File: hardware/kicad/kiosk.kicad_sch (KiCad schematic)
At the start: 16 parts, among them J10 Jack 5V rail 1, J11 Jack 5V rail 2, J13 PCF8574 - han day tu hang P, J14 LCD microSD - lo cho, chua no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, J3 LCD 4.0in ST7796S + GT911, J4 VL53L1X, J5 PCF8574 - de cam 4 chan nguon, J6 DS3231, J7 MAX98357A, J9 SG90 servo, U1 ESP32-S3-CAM N16R8

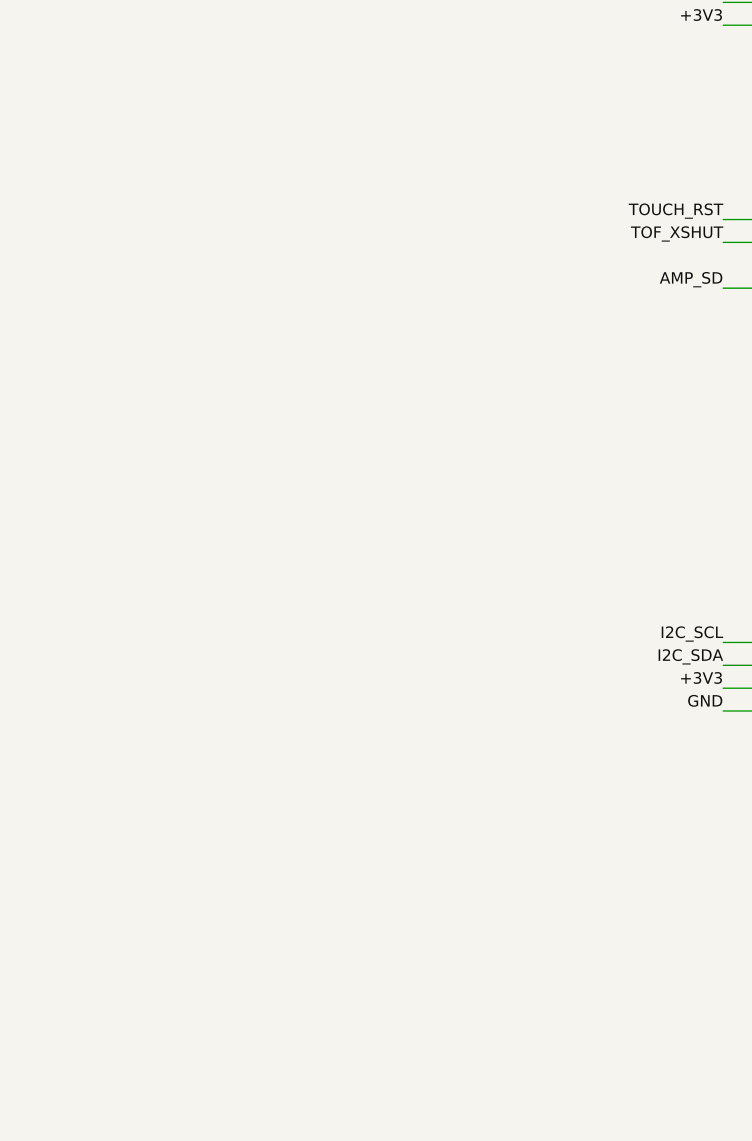
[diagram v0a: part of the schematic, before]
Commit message: feat(hardware): add two USB power inlets beside the terminals
A bench supply now reaches the board over USB as well as through the screw
terminals. Each inlet is two parts: four holes with no net on them at all,
which a breakout solders onto so it cannot come loose, and a pair of holes
above it carrying the rail, which two short wires from the breakout's VBUS
and GND reach.

The anchor row carries no net on purpose. Cheap USB breakouts follow no pin
standard - micro-USB is usually five pins, USB-C ships as two, six and
sixteen, and VBUS and GND sit adjacent on some and at opposite ends on
others - so any net assigned there would encode a guess. Wiring the power
by hand costs two solder joints and works with every one of them.

USB-C feeds rail 1 and micro-USB feeds rail 2, because a C connector is
rated 3 A against rail 1's 1.34 A peak while micro-B is rated 1.8 A and
suits the servo's 0.7 A.

C1, J10 and J11 move 3 mm right to open the pocket. It is a translation, so
every distance the section 2.5 rules name is unchanged, including the
11.5 mm between the two grounds.

Task: E14-T8
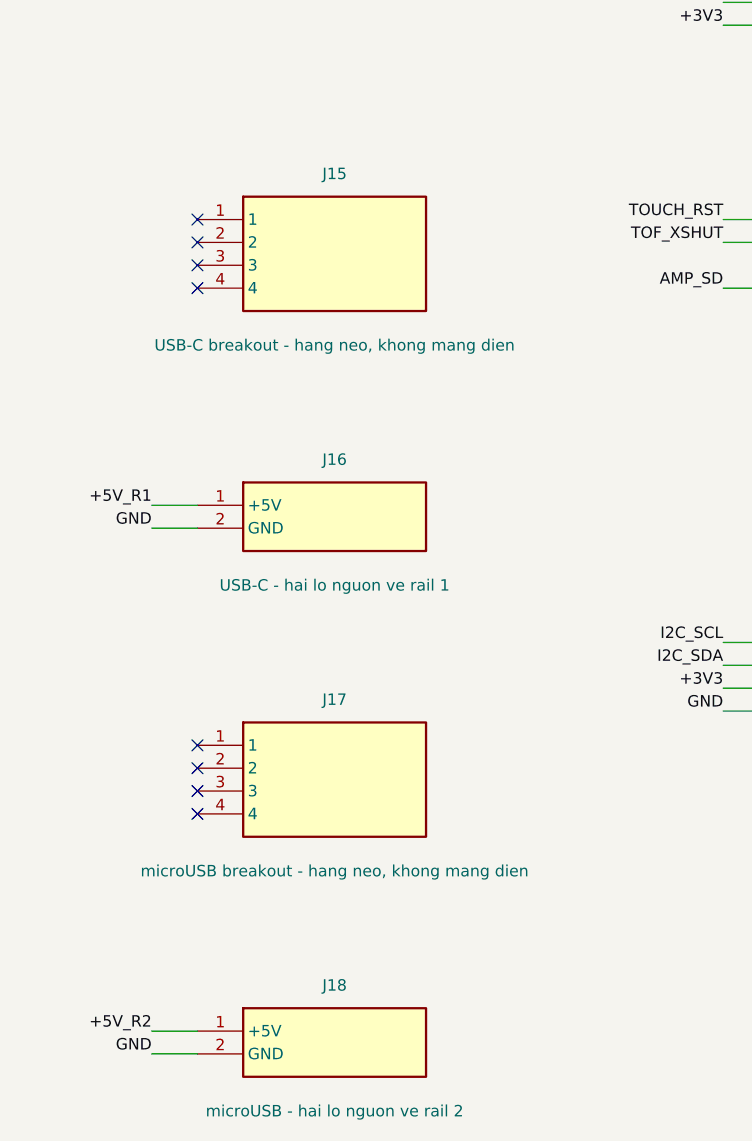
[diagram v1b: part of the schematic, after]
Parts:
- added J15: USB-C breakout - hang neo, khong mang dien, Connector_PinHeader_2.54mm:PinHeader_1x04_P2.54mm_Vertical, symbol kiosk:J15
- added J16: USB-C - hai lo nguon ve rail 1, Connector_PinHeader_2.54mm:PinHeader_1x02_P2.54mm_Vertical, symbol kiosk:J16
- added J17: microUSB breakout - hang neo, khong mang dien, Connector_PinHeader_2.54mm:PinHeader_1x04_P2.54mm_Vertical, symbol kiosk:J17
- added J18: microUSB - hai lo nguon ve rail 2, Connector_PinHeader_2.54mm:PinHeader_1x02_P2.54mm_Vertical, symbol kiosk:J18
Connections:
- net +5V_R1: now also J16.1 (+5V)
- net +5V_R2: now also J18.1 (+5V)
- net GND: now also J16.2 (GND), J18.2 (GND)
- no-connect marks 36 -> 44
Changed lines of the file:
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@@
     (effects (font (size 1.27 1.27)) (justify left bottom))
+)
+  (symbol (lib_id "kiosk:J15") (at 48.26 182.88 0) (unit 1)
+    (exclude_from_sim no) (in_bom yes) (on_board yes) (dnp no)
+    (property "Reference" "J15" (at 48.26 173.98999999999998 0) (effects (font (size 1.27 1.27))))
+    (property "Value" "USB-C breakout - hang neo, khong mang dien" (at 48.26 193.04 0) (effects (font (size 1.27 1.27))))
+    (property "Footprint" "Connector_PinHeader_2.54mm:PinHeader_1x04_P2.54mm_Vertical" (at 48.26 182.88 0)
+      (effects (font (size 1.27 1.27)) hide))
+    (property "Datasheet" "" (at 48.26 182.88 0) (effects (font (size 1.27 1.27)) hide))
+    (pin "1")
+    (pin "2")
+    (pin "3")
+    (pin "4")
+    (instances
+      (project "kiosk"
+        (path "/b0a1c2d3-0000-4000-8000-000000000001" (reference "J15") (unit 1))
+      )
+    )
+  )
+  (no_connect (at 33.019999999999996 179.07))
+  (no_connect (at 33.019999999999996 181.60999999999999))
+  (no_connect (at 33.019999999999996 184.15))
+  (no_connect (at 33.019999999999996 186.69))
+  (symbol (lib_id "kiosk:J16") (at 48.26 212.09 0) (unit 1)
+    (exclude_from_sim no) (in_bom yes) (on_board yes) (dnp no)
+    (property "Reference" "J16" (at 48.26 205.73999999999998 0) (effects (font (size 1.27 1.27))))
+    (property "Value" "USB-C - hai lo nguon ve rail 1" (at 48.26 219.71 0) (effects (font (size 1.27 1.27))))
+    (property "Footprint" "Connector_PinHeader_2.54mm:PinHeader_1x02_P2.54mm_Vertical" (at 48.26 212.09 0)
+      (effects (font (size 1.27 1.27)) hide))
+    (property "Datasheet" "" (at 48.26 212.09 0) (effects (font (size 1.27 1.27)) hide))
+    (pin "1")
+    (pin "2")
+    (instances
+      (project "kiosk"
+        (path "/b0a1c2d3-0000-4000-8000-000000000001" (reference "J16") (unit 1))
+      )
+    )
+  )
+  (wire (pts (xy 33.019999999999996 210.82) (xy 27.939999999999998 210.82))
+    (stroke (width 0) (type default)))
+  (label "+5V_R1" (at 27.939999999999998 210.82 180)
+    (effects (font (size 1.27 1.27)) (justify right bottom))
+)
+  (wire (pts (xy 33.019999999999996 213.35999999999999) (xy 27.939999999999998 213.35999999999999))
+    (stroke (width 0) (type default)))
+  (label "GND" (at 27.939999999999998 213.35999999999999 180)
+    (effects (font (size 1.27 1.27)) (justify right bottom))
+)
+  (symbol (lib_id "kiosk:J17") (at 48.26 241.3 0) (unit 1)
+    (exclude_from_sim no) (in_bom yes) (on_board yes) (dnp no)
+    (property "Reference" "J17" (at 48.26 232.41 0) (effects (font (size 1.27 1.27))))
+    (property "Value" "microUSB breakout - hang neo, khong mang dien" (at 48.26 251.46 0) (effects (font (size 1.27 1.27))))
+    (property "Footprint" "Connector_PinHeader_2.54mm:PinHeader_1x04_P2.54mm_Vertical" (at 48.26 241.3 0)
+      (effects (font (size 1.27 1.27)) hide))
+    (property "Datasheet" "" (at 48.26 241.3 0) (effects (font (size 1.27 1.27)) hide))
+    (pin "1")
+    (pin "2")
+    (pin "3")
+    (pin "4")
+    (instances
+      (project "kiosk"
+        (path "/b0a1c2d3-0000-4000-8000-000000000001" (reference "J17") (unit 1))
+      )
+    )
+  )
+  (no_connect (at 33.019999999999996 237.49))
+  (no_connect (at 33.019999999999996 240.03))
+  (no_connect (at 33.019999999999996 242.57000000000002))
+  (no_connect (at 33.019999999999996 245.11))
+  (symbol (lib_id "kiosk:J18") (at 48.26 270.51 0) (unit 1)
+    (exclude_from_sim no) (in_bom yes) (on_board yes) (dnp no)
+    (property "Reference" "J18" (at 48.26 264.16 0) (effects (font (size 1.27 1.27))))
+    (property "Value" "microUSB - hai lo nguon ve rail 2" (at 48.26 278.13 0) (effects (font (size 1.27 1.27))))
+    (property "Footprint" "Connector_PinHeader_2.54mm:PinHeader_1x02_P2.54mm_Vertical" (at 48.26 270.51 0)
+      (effects (font (size 1.27 1.27)) hide))
+    (property "Datasheet" "" (at 48.26 270.51 0) (effects (font (size 1.27 1.27)) hide))
+    (pin "1")
+    (pin "2")
+    (instances
+      (project "kiosk"
+        (path "/b0a1c2d3-0000-4000-8000-000000000001" (reference "J18") (unit 1))
+      )
+    )
+  )
+  (wire (pts (xy 33.019999999999996 269.24) (xy 27.939999999999998 269.24))
+    (stroke (width 0) (type default)))
+  (label "+5V_R2" (at 27.939999999999998 269.24 180)
+    (effects (font (size 1.27 1.27)) (justify right bottom))
+)
+  (wire (pts (xy 33.019999999999996 271.78000000000003) (xy 27.939999999999998 271.78000000000003))
+    (stroke (width 0) (type default)))
+  (label "GND" (at 27.939999999999998 271.78000000000003 180)
+    (effects (font (size 1.27 1.27)) (justify right bottom))
 )
   (symbol (lib_id "kiosk:J3") (at 111.76 48.26 0) (unit 1)

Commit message: feat(hardware): hold each USB breakout on a 2.54 solder grid
A single row of holes bets that the breakout's pins land exactly there, and
that bet has two unmeasured numbers behind it: how many pins the row has and
how far it sits from the module edge. A grid at the same pitch as the pins
takes no such bet - slide the module until the row drops into holes, solder,
leave the rest empty - and it survives swapping the breakout for another.

Each landing is a 4x5 field of bare holes, 20 per module. J15 and J17 carry
no net at all, so like the four screw holes they never appear on the
schematic; power still arrives on two wires run up to J16 and J18.

Placing one footprint twice exposed a latent fault: place() kept whatever
uuid the library file carried, so the two grids and the devkit shipped 26
uuids shared by 74 nodes. Every node now takes a uuid keyed on the reference
that owns it.

Task: E14-T8
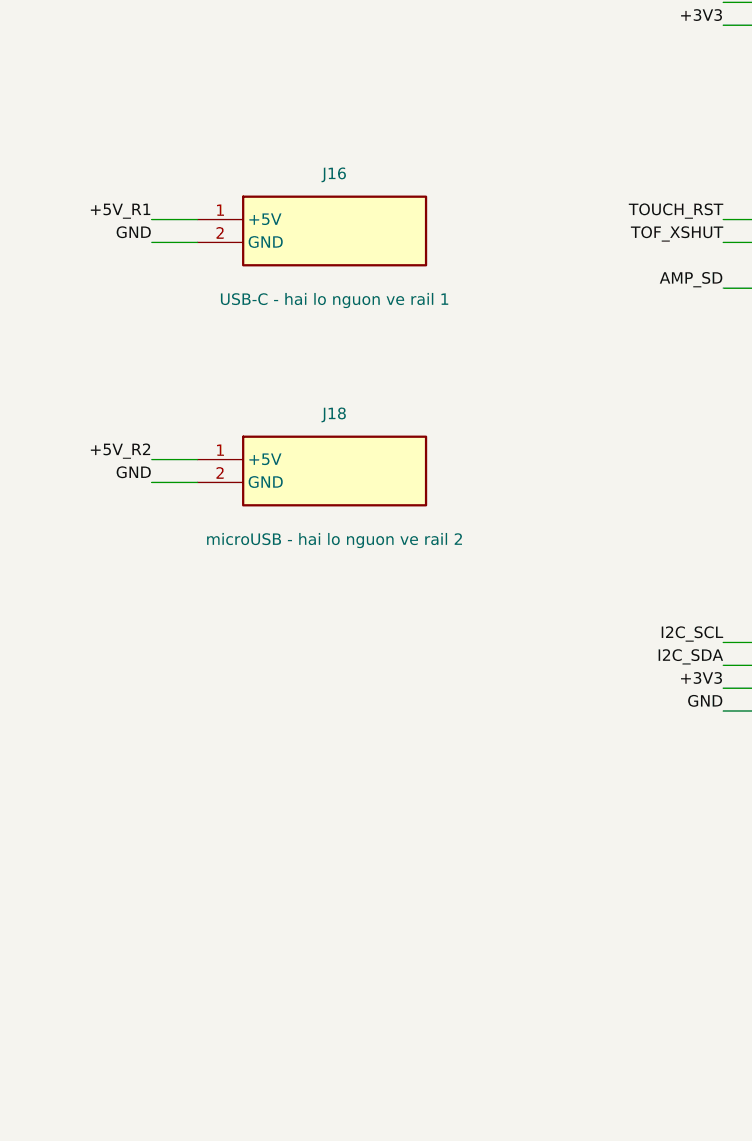
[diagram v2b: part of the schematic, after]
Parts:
- removed J15: USB-C breakout - hang neo, khong mang dien, Connector_PinHeader_2.54mm:PinHeader_1x04_P2.54mm_Vertical, symbol kiosk:J15
- removed J17: microUSB breakout - hang neo, khong mang dien, Connector_PinHeader_2.54mm:PinHeader_1x04_P2.54mm_Vertical, symbol kiosk:J17
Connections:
- no-connect marks 44 -> 36
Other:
- moved on the sheet: J16, J18
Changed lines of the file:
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@@
     (effects (font (size 1.27 1.27)) (justify left bottom))
 )
-  (symbol (lib_id "kiosk:J15") (at 48.26 182.88 0) (unit 1)
+  (symbol (lib_id "kiosk:J16") (at 48.26 180.34 0) (unit 1)
     (exclude_from_sim no) (in_bom yes) (on_board yes) (dnp no)
-    (property "Reference" "J15" (at 48.26 173.98999999999998 0) (effects (font (size 1.27 1.27))))
-    (property "Value" "USB-C breakout - hang neo, khong mang dien" (at 48.26 193.04 0) (effects (font (size 1.27 1.27))))
-    (property "Footprint" "Connector_PinHeader_2.54mm:PinHeader_1x04_P2.54mm_Vertical" (at 48.26 182.88 0)
+    (property "Reference" "J16" (at 48.26 173.98999999999998 0) (effects (font (size 1.27 1.27))))
+    (property "Value" "USB-C - hai lo nguon ve rail 1" (at 48.26 187.96 0) (effects (font (size 1.27 1.27))))
+    (property "Footprint" "Connector_PinHeader_2.54mm:PinHeader_1x02_P2.54mm_Vertical" (at 48.26 180.34 0)
       (effects (font (size 1.27 1.27)) hide))
-    (property "Datasheet" "" (at 48.26 182.88 0) (effects (font (size 1.27 1.27)) hide))
-    (pin "1")
-    (pin "2")
-    (pin "3")
-    (pin "4")
-    (instances
-      (project "kiosk"
-        (path "/b0a1c2d3-0000-4000-8000-000000000001" (reference "J15") (unit 1))
-      )
-    )
-  )
-  (no_connect (at 33.019999999999996 179.07))
-  (no_connect (at 33.019999999999996 181.60999999999999))
-  (no_connect (at 33.019999999999996 184.15))
-  (no_connect (at 33.019999999999996 186.69))
-  (symbol (lib_id "kiosk:J16") (at 48.26 212.09 0) (unit 1)
-    (exclude_from_sim no) (in_bom yes) (on_board yes) (dnp no)
-    (property "Reference" "J16" (at 48.26 205.73999999999998 0) (effects (font (size 1.27 1.27))))
-    (property "Value" "USB-C - hai lo nguon ve rail 1" (at 48.26 219.71 0) (effects (font (size 1.27 1.27))))
-    (property "Footprint" "Connector_PinHeader_2.54mm:PinHeader_1x02_P2.54mm_Vertical" (at 48.26 212.09 0)
-      (effects (font (size 1.27 1.27)) hide))
-    (property "Datasheet" "" (at 48.26 212.09 0) (effects (font (size 1.27 1.27)) hide))
+    (property "Datasheet" "" (at 48.26 180.34 0) (effects (font (size 1.27 1.27)) hide))
     (pin "1")
     (pin "2")
@@
     )
   )
-  (wire (pts (xy 33.019999999999996 210.82) (xy 27.939999999999998 210.82))
+  (wire (pts (xy 33.019999999999996 179.07) (xy 27.939999999999998 179.07))
     (stroke (width 0) (type default)))
-  (label "+5V_R1" (at 27.939999999999998 210.82 180)
+  (label "+5V_R1" (at 27.939999999999998 179.07 180)
     (effects (font (size 1.27 1.27)) (justify right bottom))
 )
-  (wire (pts (xy 33.019999999999996 213.35999999999999) (xy 27.939999999999998 213.35999999999999))
+  (wire (pts (xy 33.019999999999996 181.60999999999999) (xy 27.939999999999998 181.60999999999999))
     (stroke (width 0) (type default)))
-  (label "GND" (at 27.939999999999998 213.35999999999999 180)
+  (label "GND" (at 27.939999999999998 181.60999999999999 180)
     (effects (font (size 1.27 1.27)) (justify right bottom))
 )
-  (symbol (lib_id "kiosk:J17") (at 48.26 241.3 0) (unit 1)
+  (symbol (lib_id "kiosk:J18") (at 48.26 207.01 0) (unit 1)
     (exclude_from_sim no) (in_bom yes) (on_board yes) (dnp no)
-    (property "Reference" "J17" (at 48.26 232.41 0) (effects (font (size 1.27 1.27))))
-    (property "Value" "microUSB breakout - hang neo, khong mang dien" (at 48.26 251.46 0) (effects (font (size 1.27 1.27))))
-    (property "Footprint" "Connector_PinHeader_2.54mm:PinHeader_1x04_P2.54mm_Vertical" (at 48.26 241.3 0)
+    (property "Reference" "J18" (at 48.26 200.65999999999997 0) (effects (font (size 1.27 1.27))))
+    (property "Value" "microUSB - hai lo nguon ve rail 2" (at 48.26 214.63 0) (effects (font (size 1.27 1.27))))
+    (property "Footprint" "Connector_PinHeader_2.54mm:PinHeader_1x02_P2.54mm_Vertical" (at 48.26 207.01 0)
       (effects (font (size 1.27 1.27)) hide))
-    (property "Datasheet" "" (at 48.26 241.3 0) (effects (font (size 1.27 1.27)) hide))
-    (pin "1")
-    (pin "2")
-    (pin "3")
-    (pin "4")
-    (instances
-      (project "kiosk"
-        (path "/b0a1c2d3-0000-4000-8000-000000000001" (reference "J17") (unit 1))
-      )
-    )
-  )
-  (no_connect (at 33.019999999999996 237.49))
-  (no_connect (at 33.019999999999996 240.03))
-  (no_connect (at 33.019999999999996 242.57000000000002))
-  (no_connect (at 33.019999999999996 245.11))
-  (symbol (lib_id "kiosk:J18") (at 48.26 270.51 0) (unit 1)
-    (exclude_from_sim no) (in_bom yes) (on_board yes) (dnp no)
-    (property "Reference" "J18" (at 48.26 264.16 0) (effects (font (size 1.27 1.27))))
-    (property "Value" "microUSB - hai lo nguon ve rail 2" (at 48.26 278.13 0) (effects (font (size 1.27 1.27))))
-    (property "Footprint" "Connector_PinHeader_2.54mm:PinHeader_1x02_P2.54mm_Vertical" (at 48.26 270.51 0)
-      (effects (font (size 1.27 1.27)) hide))
-    (property "Datasheet" "" (at 48.26 270.51 0) (effects (font (size 1.27 1.27)) hide))
+    (property "Datasheet" "" (at 48.26 207.01 0) (effects (font (size 1.27 1.27)) hide))
     (pin "1")
     (pin "2")
@@
     )
   )
-  (wire (pts (xy 33.019999999999996 269.24) (xy 27.939999999999998 269.24))
+  (wire (pts (xy 33.019999999999996 205.73999999999998) (xy 27.939999999999998 205.73999999999998))
     (stroke (width 0) (type default)))
-  (label "+5V_R2" (at 27.939999999999998 269.24 180)
+  (label "+5V_R2" (at 27.939999999999998 205.73999999999998 180)
     (effects (font (size 1.27 1.27)) (justify right bottom))
 )
-  (wire (pts (xy 33.019999999999996 271.78000000000003) (xy 27.939999999999998 271.78000000000003))
+  (wire (pts (xy 33.019999999999996 208.27999999999997) (xy 27.939999999999998 208.27999999999997))
     (stroke (width 0) (type default)))
-  (label "GND" (at 27.939999999999998 271.78000000000003 180)
+  (label "GND" (at 27.939999999999998 208.27999999999997 180)
     (effects (font (size 1.27 1.27)) (justify right bottom))
 )

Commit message: fix(hardware): place the panel screw holes on the pattern measured off it
The four holes measure 55.0 x 102.0 mm centre to centre, so they sit 3.00 mm
in from the long edge and 2.50 mm in from the short one. The code held a
single inset for both and guessed it at 3.5. J3 drops 1 mm so the panel
still lands on y 7..114 and the top row of module outlines keeps the line
section 2.3I puts them on.

A second measurement checks the first: the two pin rows are 104 mm apart,
which is what 107 - 1.5 - 1.5 predicts from the hole pitch read centre to
centre. Read outer edge to outer edge instead and the same chain gives
100.5, so the row spacing settles which way the caliper was held.

Two faults the move brought out. Pin 1 of a header is a square pad and its
corners reach 0.35 mm further than the circle the router drew around it,
which only showed once something came close; pad reach is now the half
diagonal for rect pads. And J14 is four bare holes, not a socket, so it
takes an in-house footprint that draws no outline - the panel body is the
only outline that means anything there, and a socket printed across it was
crowding it.

Task: E14-T9
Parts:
- J14: footprint Connector_PinHeader_2.54mm:PinHeader_1x04_P2.54mm_Vertical -> kiosk:BareHoles_1x04_P2.54mm
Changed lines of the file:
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@@
     (property "Reference" "J14" (at 111.76 81.28 0) (effects (font (size 1.27 1.27))))
     (property "Value" "LCD microSD - lo cho, chua noi day" (at 111.76 100.33 0) (effects (font (size 1.27 1.27))))
-    (property "Footprint" "Connector_PinHeader_2.54mm:PinHeader_1x04_P2.54mm_Vertical" (at 111.76 90.17 0)
+    (property "Footprint" "kiosk:BareHoles_1x04_P2.54mm" (at 111.76 90.17 0)
       (effects (font (size 1.27 1.27)) hide))
     (property "Datasheet" "" (at 111.76 90.17 0) (effects (font (size 1.27 1.27)) hide))
